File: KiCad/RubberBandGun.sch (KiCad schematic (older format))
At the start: 21 parts

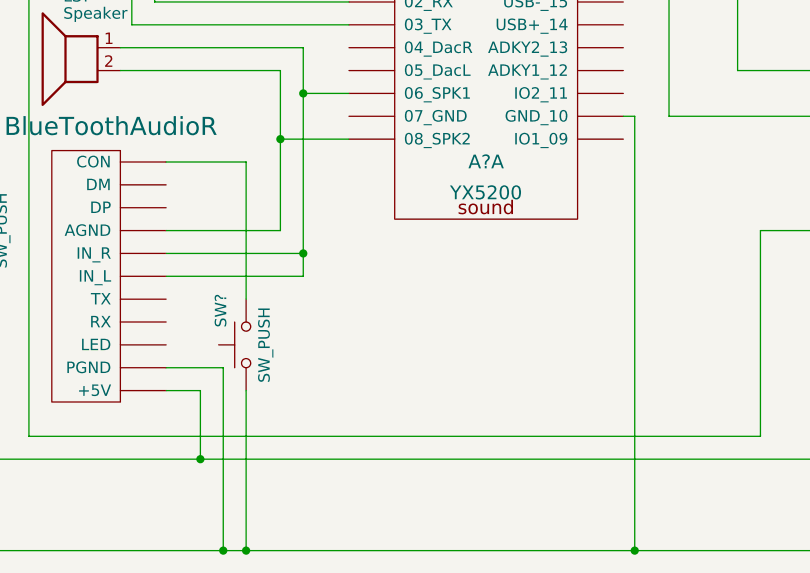
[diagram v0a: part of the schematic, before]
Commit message: add programming I/F for Bluetooth board
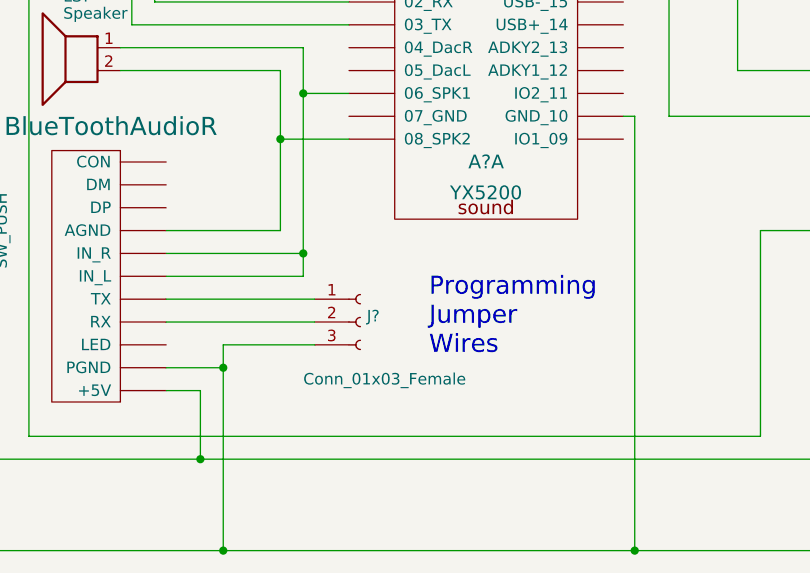
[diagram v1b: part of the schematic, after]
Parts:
- removed SW?: SW_PUSH, symbol switches:SW_Push
- added J?: Conn_01x03_Female, symbol conn:Conn_01x03_Female
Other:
- note added: "Programming\nJumper\nWires"
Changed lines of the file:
@@
 Sheet 1 3
 Title "FOOF Rubber Band Gun"
-Date "2020-08-26"
+Date "2020-09-04"
 Rev "---"
 Comp ""
@@
 Connection ~ 5250 6400
 Wire Wire Line
-	5250 6400 5350 6400
-Wire Wire Line
 	5000 1250 8000 1250
 Wire Wire Line
@@
 Wire Wire Line
 	7750 1350 8000 1350
-$Comp
-L switches:SW_Push SW?
-U 1 1 5F4922EE
-P 5350 5500
-F 0 "SW?" H 5500 5610 50  0000 C CNN
-F 1 "SW_PUSH" H 5350 5420 50  0000 C CNN
-F 2 "" H 5350 5500 60  0000 C CNN
-F 3 "" H 5350 5500 60  0000 C CNN
-	1    5350 5500
-	0    -1   -1   0
-$EndComp
-Wire Wire Line
-	5000 4700 5350 4700
-Wire Wire Line
-	5350 4700 5350 5300
-Wire Wire Line
-	5350 5700 5350 6400
-Connection ~ 5350 6400
-Wire Wire Line
-	5350 6400 7050 6400
 $Comp
 L Device:C C?
@@
 Wire Wire Line
 	5500 4600 5500 5000
+Wire Wire Line
+	5250 6400 7050 6400
+$Comp
+L conn:Conn_01x03_Female J?
+U 1 1 5F539118
+P 5850 5400
+F 0 "J?" H 5878 5426 50  0000 L CNN
+F 1 "Conn_01x03_Female" H 5600 5150 50  0000 L CNN
+F 2 "" H 5850 5400 50  0001 C CNN
+F 3 "~" H 5850 5400 50  0001 C CNN
+	1    5850 5400
+	1    0    0    -1
+$EndComp
+Wire Wire Line
+	5000 5300 5650 5300
+Wire Wire Line
+	5000 5400 5650 5400
+Wire Wire Line
+	5250 5600 5250 5500
+Wire Wire Line
+	5250 5500 5650 5500
+Connection ~ 5250 5600
+Text Notes 6150 5550 0    79   ~ 0
+Programming\nJumper\nWires
 $EndSCHEMATC

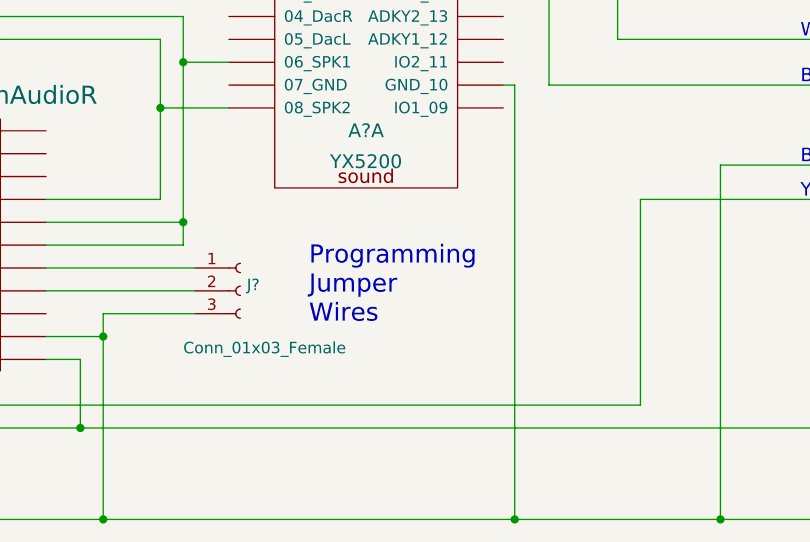
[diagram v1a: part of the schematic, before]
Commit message: tweaks to schematic for programming Bluetooth
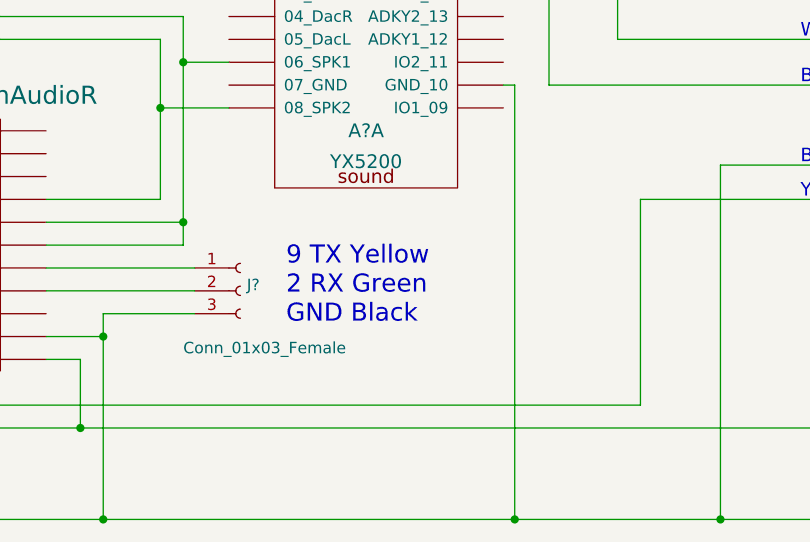
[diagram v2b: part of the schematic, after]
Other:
- note added: "9 TX Yellow\n2 RX Green\nGND Black"
- note removed: "Programming\nJumper\nWires"
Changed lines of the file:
@@
 Sheet 1 3
 Title "FOOF Rubber Band Gun"
-Date "2020-09-04"
+Date "2020-09-05"
 Rev "---"
 Comp ""
@@
 	5250 5500 5650 5500
 Connection ~ 5250 5600
-Text Notes 6150 5550 0    79   ~ 0
-Programming\nJumper\nWires
+Text Notes 6050 5550 0    79   ~ 0
+9 TX Yellow\n2 RX Green\nGND Black
 $EndSCHEMATC

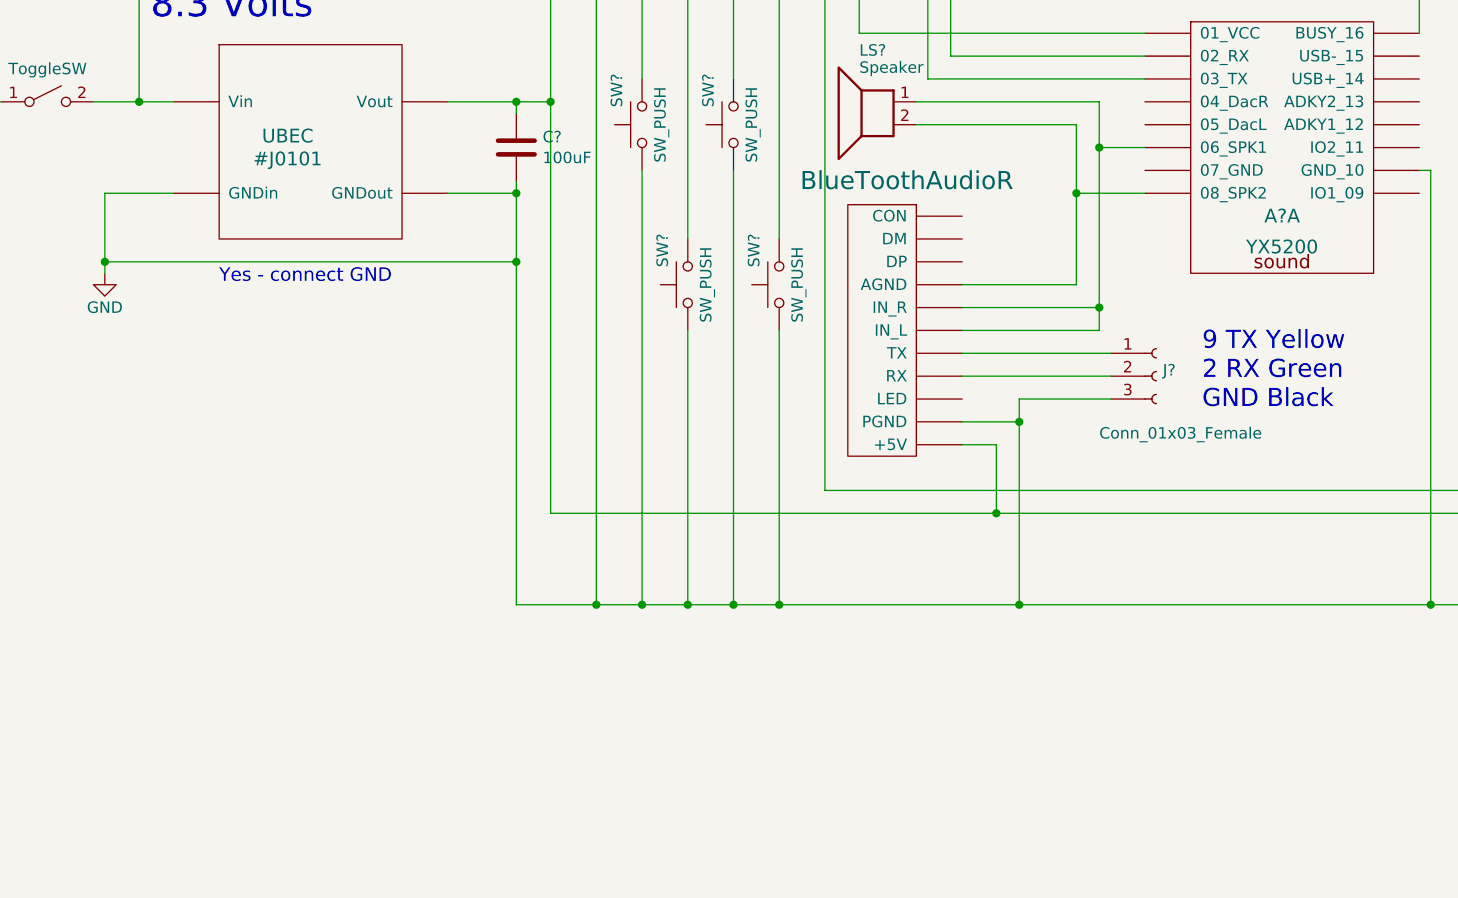
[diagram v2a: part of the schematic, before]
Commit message: add Programming Arduino for temp connection to program KCX_BT_EMITTER
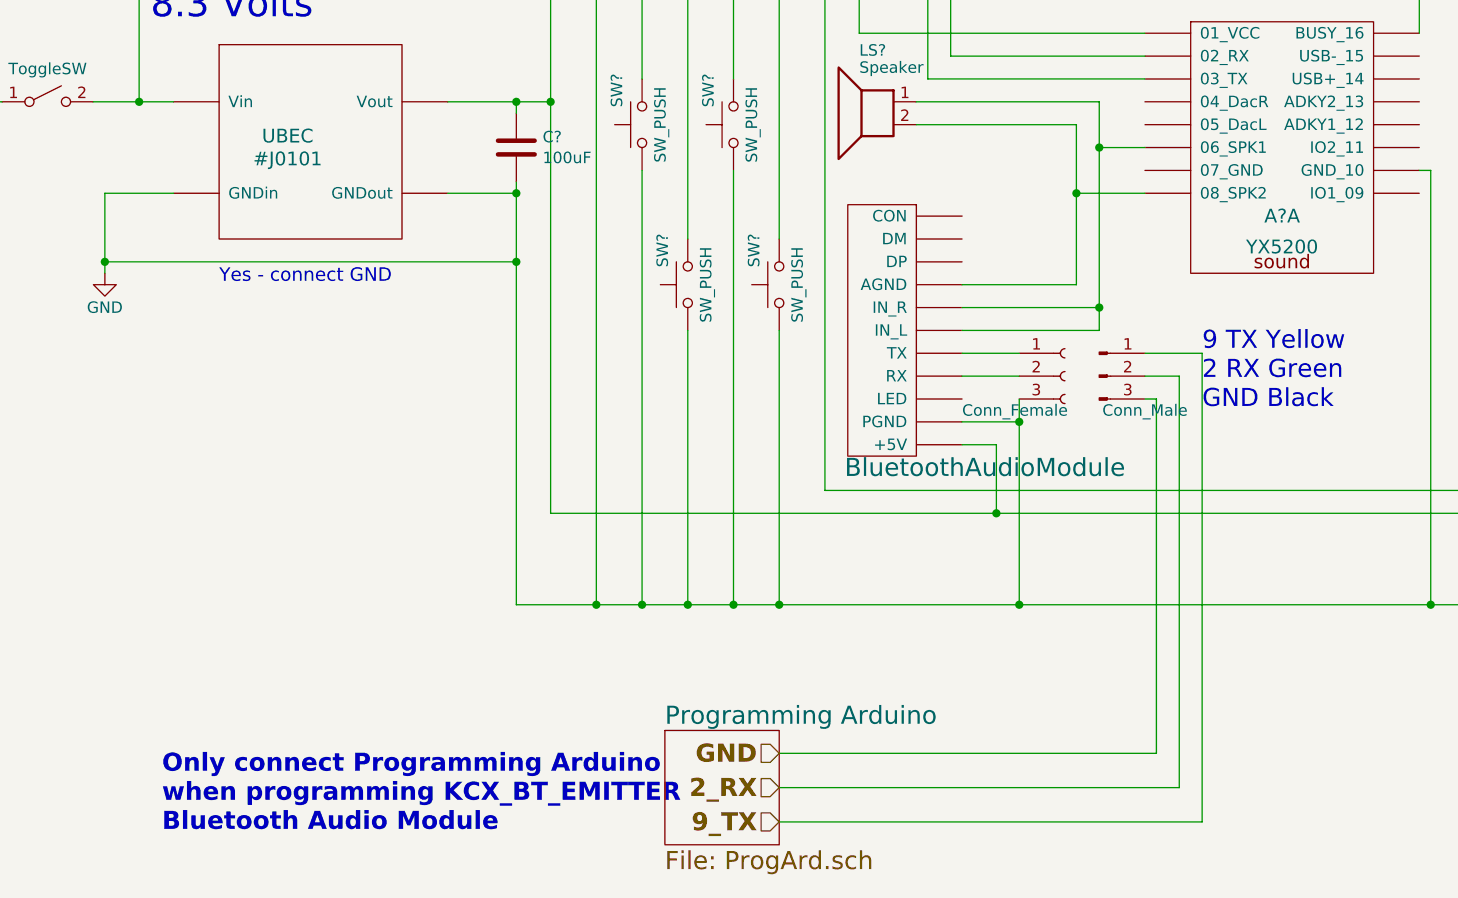
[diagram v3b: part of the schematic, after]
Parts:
- added J?: Conn_Male, symbol conn:Conn_01x03_Male
- J?: value Conn_01x03_Female -> Conn_Female
- U?: value BlueToothAudioR -> BluetoothAudioModule
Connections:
- net labels added: 2_RX, 9_TX
- wire segments 136 -> 144
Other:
- note added: "Only connect Programming Arduino\nwhen programming KCX_BT_EMITTER\nBluetooth Audio Module"
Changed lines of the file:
@@
 $Descr A 11000 8500
 encoding utf-8
-Sheet 1 3
+Sheet 1 4
 Title "FOOF Rubber Band Gun"
 Date "2020-09-05"
@@
 P 4700 4650
 F 0 "U?" H 4700 4650 79  0001 C CNN
-F 1 "BlueToothAudioR" H 4758 4755 79  0000 C CNN
+F 1 "BluetoothAudioModule" H 5100 3500 79  0000 C CNN
 F 2 "" H 4700 4650 79  0001 C CNN
 F 3 "" H 4700 4650 79  0001 C CNN
@@
 L conn:Conn_01x03_Female J?
 U 1 1 5F539118
-P 5850 5400
-F 0 "J?" H 5878 5426 50  0000 L CNN
-F 1 "Conn_01x03_Female" H 5600 5150 50  0000 L CNN
-F 2 "" H 5850 5400 50  0001 C CNN
-F 3 "~" H 5850 5400 50  0001 C CNN
-	1    5850 5400
-	1    0    0    -1
-$EndComp
-Wire Wire Line
-	5000 5300 5650 5300
-Wire Wire Line
-	5000 5400 5650 5400
+P 5450 5400
+F 0 "J?" H 5478 5426 50  0001 L CNN
+F 1 "Conn_Female" H 5000 5250 50  0000 L CNN
+F 2 "" H 5450 5400 50  0001 C CNN
+F 3 "~" H 5450 5400 50  0001 C CNN
+	1    5450 5400
+	1    0    0    -1
+$EndComp
 Wire Wire Line
 	5250 5600 5250 5500
-Wire Wire Line
-	5250 5500 5650 5500
 Connection ~ 5250 5600
 Text Notes 6050 5550 0    79   ~ 0
 9 TX Yellow\n2 RX Green\nGND Black
+$Sheet
+S 3700 6950 500  500
+U 5F557D0B
+F0 "Programming Arduino" 79
+F1 "ProgArd.sch" 79
+$EndSheet
+Wire Wire Line
+	5000 5300 5250 5300
+Wire Wire Line
+	5000 5400 5250 5400
+Text HLabel 4200 7350 0    79   Input ~ 16
+9_TX
+Text HLabel 4200 7200 0    79   Input ~ 16
+2_RX
+Text HLabel 4200 7050 0    79   Input ~ 16
+GND
+$Comp
+L conn:Conn_01x03_Male J?
+U 1 1 5F5917B1
+P 5600 5400
+F 0 "J?" H 5708 5681 50  0001 C CNN
+F 1 "Conn_Male" H 5800 5250 50  0000 C CNN
+F 2 "" H 5600 5400 50  0001 C CNN
+F 3 "~" H 5600 5400 50  0001 C CNN
+	1    5600 5400
+	1    0    0    -1
+$EndComp
+Wire Wire Line
+	4200 7050 5850 7050
+Wire Wire Line
+	4200 7200 5950 7200
+Wire Wire Line
+	5950 7200 5950 5400
+Wire Wire Line
+	5950 5400 5800 5400
+Text Notes 1500 7400 0    79   ~ 16
+Only connect Programming Arduino\nwhen programming KCX_BT_EMITTER\nBluetooth Audio Module
+Wire Wire Line
+	5850 7050 5850 5500
+Wire Wire Line
+	6050 5300 6050 7350
+Wire Wire Line
+	4200 7350 6050 7350
+Wire Wire Line
+	6050 5300 5800 5300
+Wire Wire Line
+	5800 5500 5850 5500
 $EndSCHEMATC

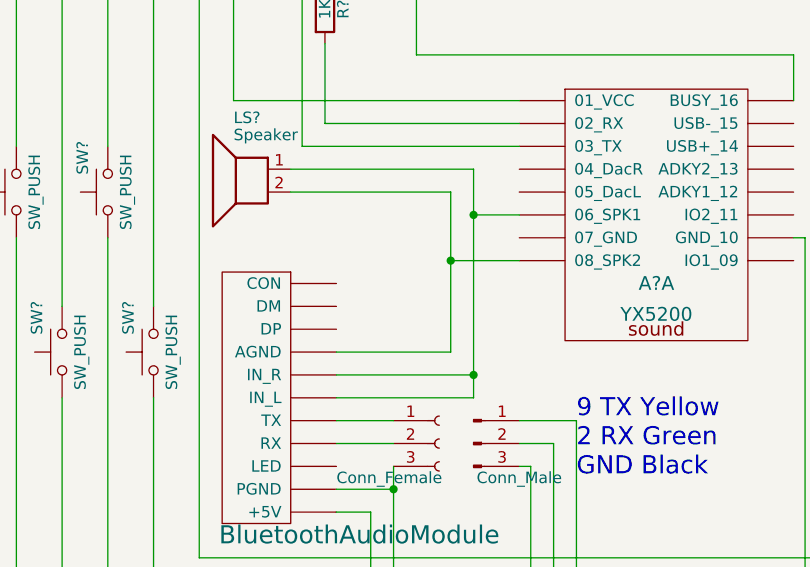
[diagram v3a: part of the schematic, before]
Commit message: separating analog ground from digital ground solved the bluetooth hum problem
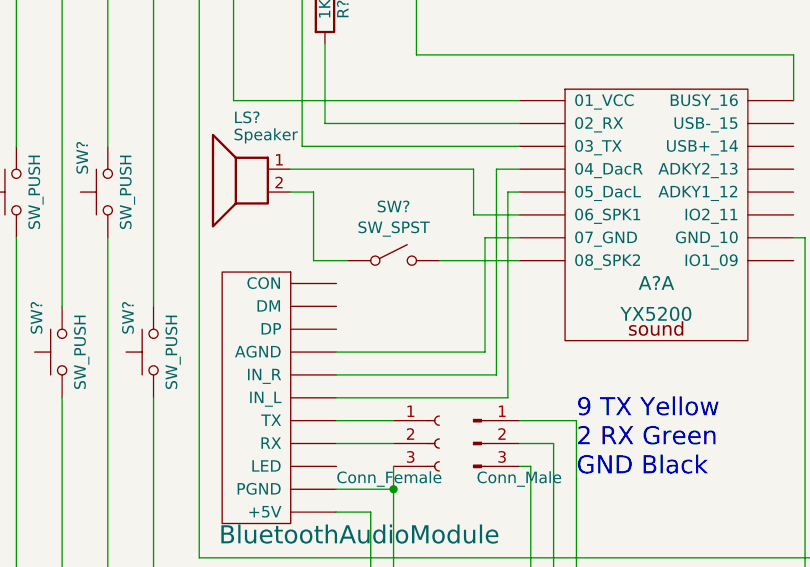
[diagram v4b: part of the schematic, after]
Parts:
- added SW?: SW_SPST, symbol mdoLibrary:SW_SPST
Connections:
- wire segments 144 -> 148
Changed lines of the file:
@@
 Wire Wire Line
 	1400 750  7500 750
-Wire Wire Line
-	5800 4400 5600 4400
-Wire Wire Line
-	5600 4400 5600 4200
-Wire Wire Line
-	5600 4200 4800 4200
-Wire Wire Line
-	5500 4300 4800 4300
 $Comp
 L mdoLibrary:BlueToothAudioR U?
@@
 Wire Wire Line
 	7600 5000 7600 5900
-Wire Wire Line
-	5000 5000 5500 5000
-Wire Wire Line
-	5600 4400 5600 5100
-Wire Wire Line
-	5600 5100 5000 5100
-Connection ~ 5600 4400
-Wire Wire Line
-	5600 5100 5600 5200
-Wire Wire Line
-	5600 5200 5000 5200
-Connection ~ 5600 5100
 Wire Wire Line
 	5000 5700 5150 5700
@@
 Wire Wire Line
 	7050 6400 7950 6400
-Wire Wire Line
-	5500 4300 5500 4600
-Wire Wire Line
-	5800 4600 5500 4600
-Connection ~ 5500 4600
-Wire Wire Line
-	5500 4600 5500 5000
 Wire Wire Line
 	5250 6400 7050 6400
@@
 Wire Wire Line
 	5800 5500 5850 5500
+Wire Wire Line
+	4900 4600 4900 4300
+Wire Wire Line
+	4900 4300 4800 4300
+Wire Wire Line
+	5800 4200 5700 4200
+Wire Wire Line
+	5800 4300 5750 4300
+Wire Wire Line
+	5800 4500 5650 4500
+Wire Wire Line
+	5700 5100 5700 4200
+Wire Wire Line
+	5000 5100 5700 5100
+Wire Wire Line
+	5750 5200 5750 4300
+Wire Wire Line
+	5000 5200 5750 5200
+Wire Wire Line
+	5650 5000 5650 4500
+Wire Wire Line
+	5000 5000 5650 5000
+$Comp
+L mdoLibrary:SW_SPST SW?
+U 1 1 5F5ADEC3
+P 5250 4600
+F 0 "SW?" H 5250 4835 50  0000 C CNN
+F 1 "SW_SPST" H 5250 4744 50  0000 C CNN
+F 2 "" H 5250 4600 50  0001 C CNN
+F 3 "" H 5250 4600 50  0001 C CNN
+	1    5250 4600
+	1    0    0    -1
+$EndComp
+Wire Wire Line
+	5800 4600 5450 4600
+Wire Wire Line
+	5050 4600 4900 4600
+Wire Wire Line
+	5800 4400 5600 4400
+Wire Wire Line
+	5600 4400 5600 4200
+Wire Wire Line
+	4800 4200 5600 4200
 $EndSCHEMATC

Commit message: use new color scheme for USB connector
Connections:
- net labels added: Green_CTL, Red_8V
- net labels removed: Blue_CTL, White_8V
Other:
- note added: "Green"
- note added: "Red"
- note removed: "Blue"
- note removed: "White"
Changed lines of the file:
@@
 Sheet 1 4
 Title "FOOF Rubber Band Gun"
-Date "2020-09-05"
+Date "2020-09-12"
 Rev "---"
 Comp ""
@@
 	8650 4500 7200 4500
 Text Notes 8300 4300 0    59   ~ 0
-White
+Red
 Text Notes 8300 4500 0    59   ~ 0
-Blue
+Green
 Text Notes 8300 4850 0    59   ~ 0
 Black
@@
 $EndSheet
 Text HLabel 8950 4300 2    59   Input ~ 0
-White_8V
+Red_8V
 Text HLabel 8950 4500 2    59   Input ~ 0
-Blue_CTL
+Green_CTL
 Text HLabel 8950 4850 2    59   Input ~ 0
 Black_GND
